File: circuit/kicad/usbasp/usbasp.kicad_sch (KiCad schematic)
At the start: 27 parts, among them J1 Conn_01x06_Male, J2 USB_B_Micro, SW1 SW_Push, SW2 SW_Push, U1 ATmega8A-A, Y1 Crystal

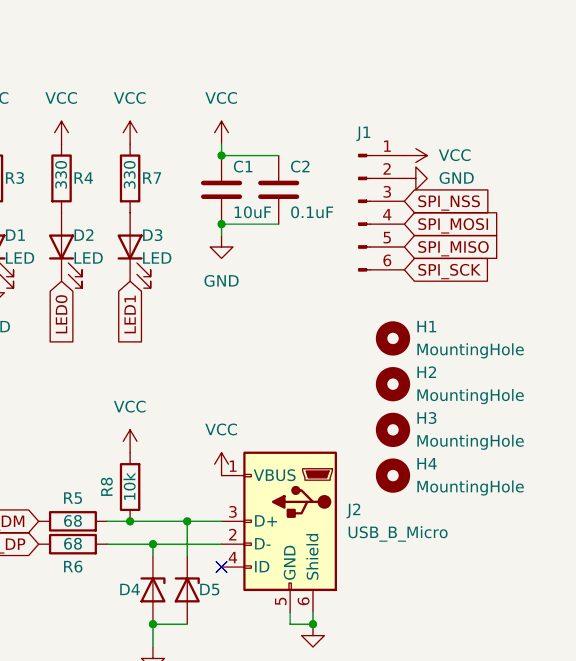
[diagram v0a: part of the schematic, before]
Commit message: Migrate Eagle-KiCAD: USBASP
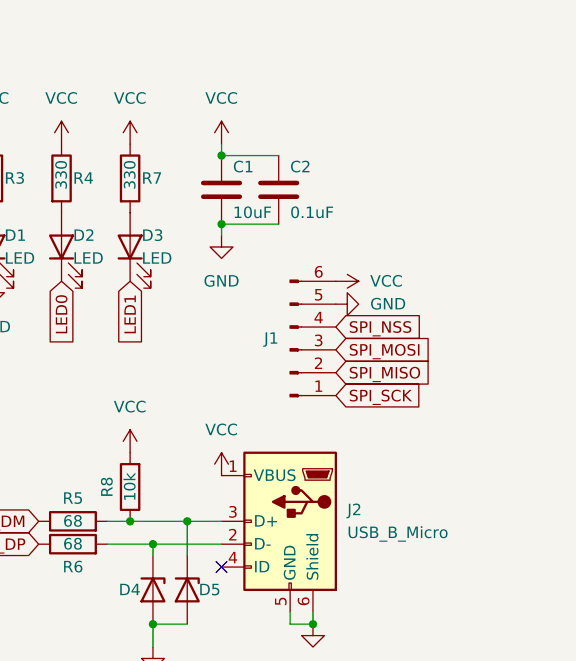
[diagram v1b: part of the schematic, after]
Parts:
- removed H1, H2, H3, H4: MountingHole, symbol Mechanical:MountingHole
- C1, C2, C3, C4: footprint (none) -> Capacitor_SMD:C_0805_2012Metric_Pad1.18x1.45mm_HandSolder
- D1, D2, D3: footprint (none) -> LED_SMD:LED_0805_2012Metric_Pad1.15x1.40mm_HandSolder
- D4, D5: footprint (none) -> Diode_SMD:D_MiniMELF_Handsoldering
- J1: footprint (none) -> Connector_PinHeader_2.54mm:PinHeader_1x06_P2.54mm_Horizontal
- J2: footprint (none) -> Connector_USB:USB_Micro-B_Wuerth_629105150521
- R1, R2, R3, R4, R5, R6, R7, R8: footprint (none) -> Resistor_SMD:R_0805_2012Metric_Pad1.20x1.40mm_HandSolder
- SW1, SW2: footprint (none) -> Button_Switch_THT:SW_PUSH_6mm
- Y1: footprint (none) -> Crystal:Crystal_HC49-4H_Vertical
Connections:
- net GND: now also J1.5 (Pin_5); no longer J1.2 (Pin_2)
- net SPI_MISO: now also J1.2 (Pin_2); no longer J1.5 (Pin_5)
- net SPI_MOSI: now also J1.3 (Pin_3); no longer J1.4 (Pin_4)
- net SPI_NSS: now also J1.4 (Pin_4); no longer J1.3 (Pin_3)
- net SPI_SCK: now also J1.1 (Pin_1); no longer J1.6 (Pin_6)
- net VCC: now also J1.6 (Pin_6); no longer J1.1 (Pin_1)
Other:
- moved on the sheet: J1
